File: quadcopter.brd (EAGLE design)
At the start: 137.2 x 137.2 mm, 69 parts, among them J4 AVR_SPI_PRG_6NS, M1 MOTOR_PADS, M2 MOTOR_PADS, M3 MOTOR_PADS, M4 MOTOR_PADS, U1 ATMEGA128RFA1

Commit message: Push Board
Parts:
- moved D6 34.8 mm to (10.2, -14.6)
- moved D5 34.5 mm to (15.6, -14.6)
- moved R5 34.5 mm to (15.6, -17.1)
- moved R6 34.5 mm to (10.2, -16.8)
- moved C7 32.5 mm to (-21.3, -20.3)
- moved C8 32.5 mm to (-23.5, -20.3)
- moved C4 30.3 mm to (-20.3, -7.94), turned to 270 degrees
- moved Y1 22.7 mm to (-18.1, -3.81), turned to 180 degrees
- moved R1 22.2 mm to (-12.1, -23.5), turned to 270 degrees
- moved C3 16.5 mm to (-13.3, -4.13)
- moved C1 13.4 mm to (-8.89, -24.1), turned to 180 degrees
- moved C27 13.3 mm to (-0.32, -4.76), turned to 180 degrees
- moved C24 11.8 mm to (-9.21, 24.1), flipped to the bottom, turned to 0 degrees
- moved C2 11.5 mm to (-14.9, -8.57)
- moved U1 7.78 mm to (-5.40, -18.1)
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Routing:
- net GND: track 0.00 -> 393.3 mm, vias 32 -> 27
- net VBAT: track 0.00 -> 342.9 mm, vias 9 -> 3
- net BAT_GND: track 0.00 -> 285.9 mm, vias 6 -> 2
- net 3.0V: track 0.00 -> 210.6 mm, vias 7 -> 11
- net RX0: track 0.00 -> 118.8 mm, vias 0 -> 4
- net PE5: track 0.00 -> 115.4 mm
- net PE4: track 0.00 -> 114.7 mm, vias 0 -> 2
- net RESET: track 0.00 -> 103.2 mm, vias 1 -> 3
- net PB5: track 0.00 -> 95.4 mm, vias 0 -> 6
- net PE3: track 0.00 -> 84.2 mm, vias 2 -> 3
- net SDA: track 0.00 -> 67.2 mm, vias 2 -> 3
- net SCL: track 0.00 -> 64.6 mm, vias 0 -> 2
- net TX0: track 0.00 -> 61.1 mm
- net TX1: track 0.00 -> 46.1 mm, vias 0 -> 2
- net MOSI: track 0.00 -> 39.6 mm
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
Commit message: Push Board
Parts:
- moved C26 0.64 mm to (-12.7, 17.1)
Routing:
- net 3.0V: track 210.6 -> 212.1 mm, vias 11 -> 12
- net GND: track 393.3 -> 394.0 mm, vias 27 -> 29
- net SDA: track 67.2 -> 67.8 mm
- net N$18: track 2.06 -> 2.64 mm
- net RX1: track 28.3 -> 28.8 mm
- net AVDD: track 12.7 -> 13.2 mm
- net DVDD: track 2.12 -> 2.62 mm

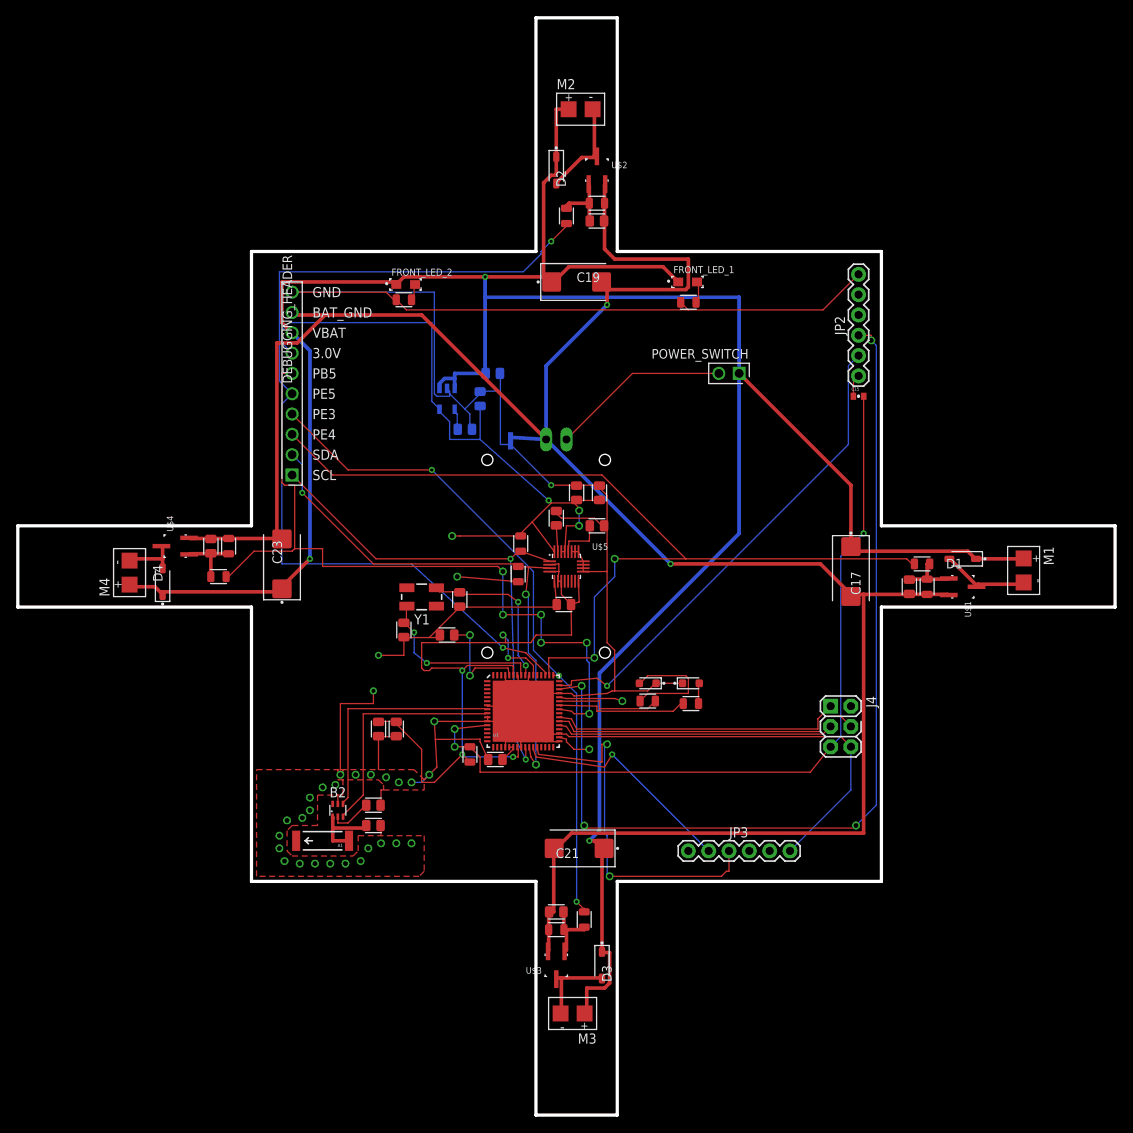
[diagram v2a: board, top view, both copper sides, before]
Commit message: added motor holes
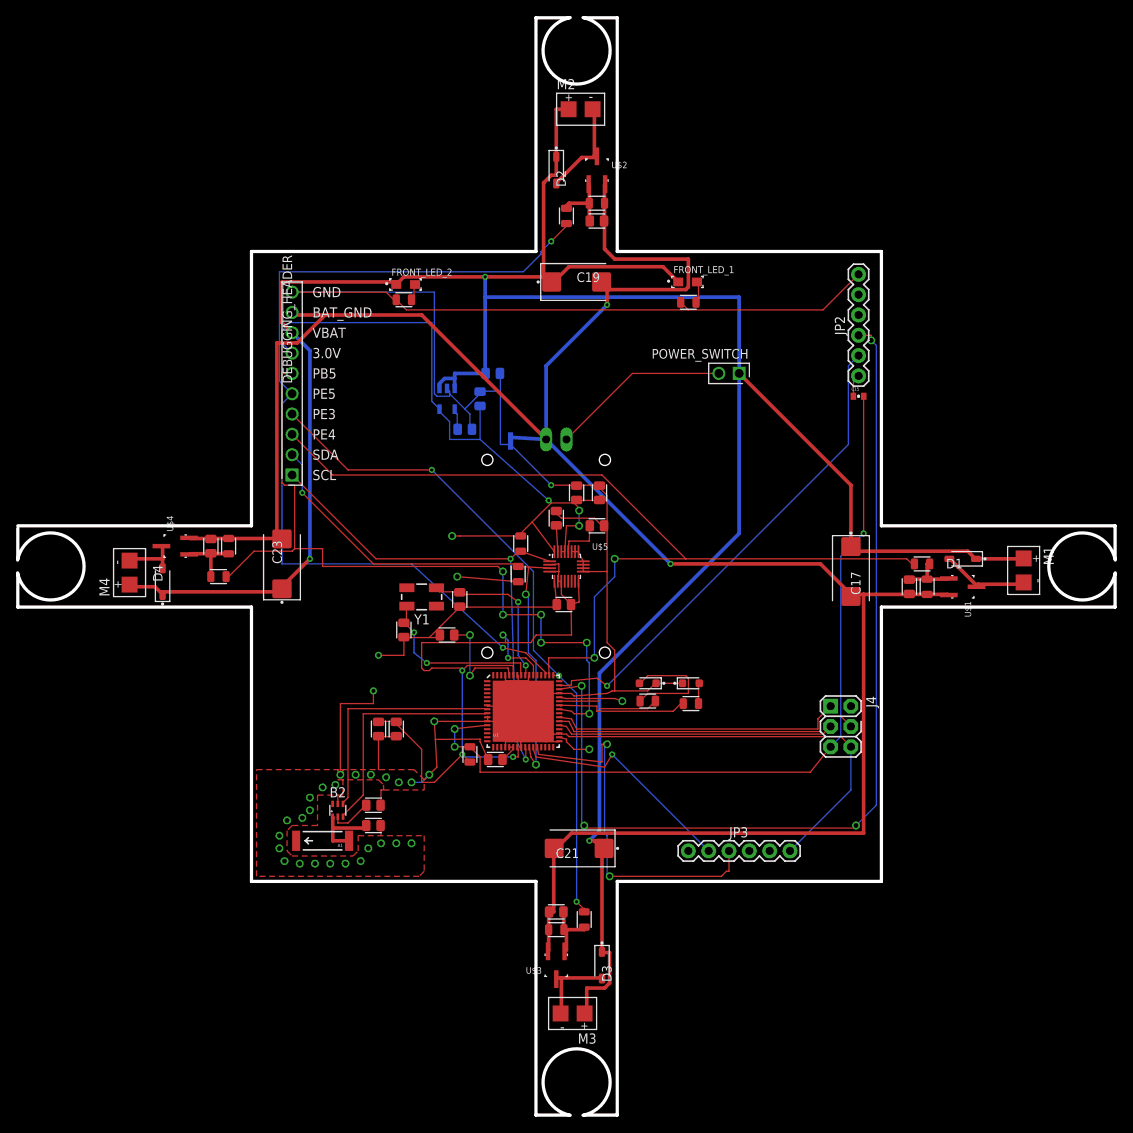
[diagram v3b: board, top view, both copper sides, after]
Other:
- outline, holes or cut-outs redrawn
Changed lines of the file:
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@@
 <wire x1="-39.37" y1="39.37" x2="-3.81" y2="39.37" width="0.4064" layer="20"/>
 <wire x1="-3.81" y1="39.37" x2="-3.81" y2="68.58" width="0.4064" layer="20"/>
-<wire x1="-3.81" y1="68.58" x2="6.35" y2="68.58" width="0.4064" layer="20"/>
 <wire x1="6.35" y1="68.58" x2="6.35" y2="39.37" width="0.4064" layer="20"/>
 <wire x1="6.35" y1="39.37" x2="39.37" y2="39.37" width="0.4064" layer="20"/>
 <wire x1="39.37" y1="39.37" x2="39.37" y2="5.08" width="0.4064" layer="20"/>
 <wire x1="39.37" y1="5.08" x2="68.58" y2="5.08" width="0.4064" layer="20"/>
-<wire x1="68.58" y1="5.08" x2="68.58" y2="-5.08" width="0.4064" layer="20"/>
 <wire x1="68.58" y1="-5.08" x2="39.37" y2="-5.08" width="0.4064" layer="20"/>
 <wire x1="39.37" y1="-5.08" x2="39.37" y2="-39.37" width="0.4064" layer="20"/>
 <wire x1="39.37" y1="-39.37" x2="6.35" y2="-39.37" width="0.4064" layer="20"/>
 <wire x1="6.35" y1="-39.37" x2="6.35" y2="-68.58" width="0.4064" layer="20"/>
-<wire x1="6.35" y1="-68.58" x2="-3.81" y2="-68.58" width="0.4064" layer="20"/>
 <wire x1="-3.81" y1="-68.58" x2="-3.81" y2="-39.37" width="0.4064" layer="20"/>
 <wire x1="-3.81" y1="-39.37" x2="-39.37" y2="-39.37" width="0.4064" layer="20"/>
 <wire x1="-39.37" y1="-39.37" x2="-39.37" y2="-5.08" width="0.4064" layer="20"/>
 <wire x1="-39.37" y1="-5.08" x2="-68.58" y2="-5.08" width="0.4064" layer="20"/>
-<wire x1="-68.58" y1="-5.08" x2="-68.58" y2="5.08" width="0.4064" layer="20"/>
 <wire x1="-68.58" y1="5.08" x2="-39.37" y2="5.08" width="0.4064" layer="20"/>
 <rectangle x1="-3.81" y1="-3.175" x2="3.81" y2="3.175" layer="42"/>
@@
 <text x="-31.75" y="13.335" size="1.27" layer="22">SDA</text>
 <text x="-31.75" y="10.795" size="1.27" layer="22">SCL</text>
+<wire x1="68.6025" y1="-0.8" x2="68.6025" y2="0.8" width="0.4064" layer="20" curve="-338"/>
+<wire x1="68.58" y1="-5.08" x2="68.58" y2="-0.9525" width="0.4064" layer="20"/>
+<wire x1="68.58" y1="0.9525" x2="68.58" y2="5.08" width="0.4064" layer="20"/>
+<wire x1="2.07" y1="68.6025" x2="0.47" y2="68.6025" width="0.4064" layer="20" curve="-338"/>
+<wire x1="-3.81" y1="68.58" x2="0.3175" y2="68.58" width="0.4064" layer="20"/>
+<wire x1="2.2225" y1="68.58" x2="6.35" y2="68.58" width="0.4064" layer="20"/>
+<wire x1="-68.6025" y1="0.8" x2="-68.6025" y2="-0.8" width="0.4064" layer="20" curve="-338"/>
+<wire x1="-68.58" y1="-5.08" x2="-68.58" y2="-0.9525" width="0.4064" layer="20"/>
+<wire x1="-68.58" y1="0.9525" x2="-68.58" y2="4.7625" width="0.4064" layer="20"/>
+<wire x1="0.47" y1="-68.6025" x2="2.07" y2="-68.6025" width="0.4064" layer="20" curve="-338"/>
+<wire x1="-3.81" y1="-68.58" x2="0.3175" y2="-68.58" width="0.4064" layer="20"/>
+<wire x1="2.2225" y1="-68.58" x2="6.35" y2="-68.58" width="0.4064" layer="20"/>
 </plain>
 <attributes>

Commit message: Design Review -- Board
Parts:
- added U$6: (no value), quadparts_jay:LE_PEPE
- added U$7: (no value), quadparts_jay:DOGE
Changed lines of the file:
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@@
 <attribute name="MPN" value="RC0805JR-07100RL" x="44.45" y="0.3175" size="1.778" layer="27" display="off"/>
 </element>
+<element name="U$6" library="quadparts_jay" package="LE_PEPE" value="" x="23.1775" y="33.02"/>
+<element name="U$7" library="quadparts_jay" package="DOGE" value="" x="-36.5125" y="-22.86"/>
 </elements>
 <signals>

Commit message: Board is done
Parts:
- removed A1: ANTENNA2SMD5, SparkFun-RF:ANTENNA-CHIP5
- removed C1, C2: 1uF, quadparts_prebuilt:CAPC2012X140_HS
- removed C3, C4: 12pF, quadparts_prebuilt:CAPC2012X140_HS
- removed D5, D6: green, quadparts_prebuilt:LEDSC125X200X120-2_HS
- removed M1, M2, M3, M4: MOTOR_PADS, Andranik-Lab4:MOTOR_PADS
- removed R1: 10K, quadparts_prebuilt:RESC2012X60_HS
- removed R5, R6: 330, quadparts_prebuilt:RESC2012X60_HS
- removed U1: ATMEGA128RFA1, SparkFun-DigitalIC:QFN-64
- removed Y1: (no value), quadparts_prebuilt:CRYSTAL-SMD-5X3
- added C13: 0.1uF, quadparts_prebuilt:CAPC2012X140_HS
- added C14, C16, C18: 12pF, quadparts_prebuilt:CAPC2012X140_HS
- added R16: 10K, quadparts_prebuilt:RESC2012X60_HS
- added U$10, U$11, U$12, U$9: MOTOR_PADS, quadparts_prebuilt:MOTOR_PADS
- added U$8: ANTENNA2SMD5, quadparts_prebuilt:ANTENNA-CHIP5
- added U2: ATMEGA128RFA1, quadparts_prebuilt:QFN-64
- added Y2: (no value), quadparts_prebuilt:CRYSTAL-SMD-5X3
- C15: value 0.1uF -> 12pF; device SparkFun-Passives:0402-CAP -> quadparts_prebuilt:CAPC2012X140_HS
- moved C8 64.2 mm to (22.4, 24.6), turned to 90 degrees
- moved C7 61.2 mm to (20.3, 24.6), turned to 90 degrees
- moved C15 58.7 mm to (-14.5, -7.75), turned to 180 degrees
- moved POWER_SWITCH 8.92 mm to (15.8, 30.9)
- moved C31 8.32 mm to (-3.68, 6.35)
- moved C28 7.61 mm to (-5.78, 6.35)
- moved B2 7.10 mm to (-21.7, -28.6)
- moved R4 4.33 mm to (15.0, 37.3), turned to 0 degrees
- moved C6 3.95 mm to (-20.8, -32.0), turned to 90 degrees
- moved R15 3.90 mm to (-19.9, 37.2)
- moved C30 3.54 mm to (0.51, 6.35), turned to 90 degrees
- moved R9 2.25 mm to (-2.22, 44.1)
- moved D3 2.22 mm to (2.22, -49.8)
- moved FRONT_LED_1 2.16 mm to (16.1, 35.5), turned to 180 degrees
- moved C21 1.90 mm to (-0.32, -35.2)
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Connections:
- removed net N$13: D6.A, R6.1
- removed net N$3: C4.1, U1.57, Y1.3
- removed net N$4: C3.1, U1.56, Y1.1
- removed net N$8: D5.A, R5.1
- new net N$12: C16.1, U2.57, Y2.1
- new net N$14: C18.1, U2.56, Y2.3
- net 3.0V: now also R16.2, U2.23, U2.34, U2.44, U2.54, U2.59; no longer R1.2, U1.23, U1.34, U1.44, U1.54, U1.59
- net A0: now also U2.63; no longer U1.63
- net A1: now also U2.64; no longer U1.64
- net A2: now also U2.1; no longer U1.1
- net A3: now also U2.2; no longer U1.2
- net A4: now also U2.3; no longer U1.3
- net A5: now also U2.4; no longer U1.4
- net A6: now also U2.5; no longer U1.5
- net A7: now also U2.6; no longer U1.6
- net AREF: now also U2.62; no longer U1.62
- net AVDD: now also C14.1, U2.60; no longer C2.1, U1.60
- net DTR: now also C13.1; no longer C15.1
- net DVDD: now also C15.1, U2.21, U2.22; no longer C1.1, U1.21, U1.22
- net FLYBACK1: now also U$10.V-; no longer M4.V-
- net FLYBACK2: now also U$9.V-; no longer M2.V-
- net FLYBACK3: now also U$12.V-; no longer M3.V-
- net FLYBACK4: now also U$11.V-; no longer M1.V-
- net GND: now also C14.2, C15.2, C16.2, C18.2, U2.10, U2.11, U2.20, U2.24, U2.33, U2.35, U2.45, U2.55, U2.58, U2.61, U2.7; no longer C1.2, C2.2, C3.2, C4.2, D5.C, D6.C, U1.10, U1.11, U1.20, U1.24, U1.33, U1.35, U1.45, U1.55, U1.58, U1.61, U1.65, U1.7
- net MISO: now also U2.39; no longer U1.39
- net MOSI: now also U2.38; no longer U1.38
- net PB4: now also U2.40; no longer U1.40
- net PB5: now also U2.41; no longer U1.41
- net PB6: now also U2.42; no longer R5.2, U1.42
- net PB7: now also U2.43; no longer R6.2, U1.43
- net PD4: now also U2.29; no longer U1.29
- net PD5: now also U2.30; no longer U1.30
- net PD6: now also U2.31; no longer U1.31
- net PD7: now also U2.32; no longer U1.32
- net PE2: now also U2.48; no longer U1.48
- net PE3: now also U2.49; no longer U1.49
- net PE4: now also U2.50; no longer U1.50
- net PE5: now also U2.51; no longer U1.51
- net PE6: now also U2.52; no longer U1.52
- net PE7: now also U2.53; no longer U1.53
- net PG0: now also U2.14; no longer U1.14
- net PG1: now also U2.15; no longer U1.15
- net PG2: now also U2.16; no longer U1.16
- net PG5: now also U2.19; no longer U1.19
- net RESET: now also C13.2, R16.1, U2.12; no longer C15.2, R1.1, U1.12
- net RFANT: now also U$8.FEED; no longer A1.FEED
- net RFN: now also U2.9; no longer U1.9
- net RFP: now also U2.8; no longer U1.8
- net RSTON: now also U2.13; no longer U1.13
- net RX0: now also U2.46; no longer U1.46
- net RX1: now also U2.27; no longer U1.27
- net SCK: now also U2.37; no longer U1.37
- net SCL: now also U2.25; no longer U1.25
- net SDA: now also U2.26; no longer U1.26
- net SSN: now also U2.36; no longer U1.36
- net TX0: now also U2.47; no longer U1.47
- net TX1: now also U2.28; no longer U1.28
- net VBAT: now also U$10.V+, U$11.V+, U$12.V+, U$9.V+; no longer M1.V+, M2.V+, M3.V+, M4.V+
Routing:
- net BAT_GND: track 285.8 -> 83.0 mm, vias 2 -> 7
- net VBAT: track 342.9 -> 141.1 mm, vias 3 -> 8
- net RX0: track 118.8 -> 75.6 mm, vias 4 -> 1
- net 3.0V: track 212.1 -> 250.3 mm, vias 12 -> 4
- net GND: track 394.0 -> 359.2 mm, vias 29 -> 46
- net N$12: track 0.00 -> 32.9 mm, vias 0 -> 2
- net N$14: track 0.00 -> 27.1 mm, vias 0 -> 2
- net SCL: track 64.3 -> 90.5 mm
- net N$3: track 22.2 -> 0.00 mm, vias 2 -> 0
- net RESET: track 103.2 -> 124.8 mm, vias 3 -> 5
- net N$4: track 20.6 -> 0.00 mm, vias 2 -> 0
- net RFP: track 29.6 -> 12.3 mm
- net PB6: track 16.8 -> 0.00 mm
- net DVDD: track 2.62 -> 19.2 mm, vias 0 -> 2
- net PE3: track 84.2 -> 100.0 mm, vias 3 -> 2
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- added copper zone on layer 15, net BAT_GND
- removed copper zone on layer 2, net N$6
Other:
- outline, holes or cut-outs redrawn
